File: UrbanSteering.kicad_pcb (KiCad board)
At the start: 2 copper layers, 144 x 78 mm, 30 parts, among them J1 DMS, J2 MAINPLUG, J3 BRAKE+THROTTLE, J4 STM32L432, J5 2.2TFT, U1 MCP2562

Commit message: started pcb layout
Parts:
- removed H7, H8: MountingHole_Pad, MountingHole:MountingHole_3.2mm_M3_Pad
- removed S6: CAN_RESISTOR_SW, dip_swtich_1pos:SW_DS04-254-2-01BK-SMT
- removed TP1: DMS2, TestPoint:TestPoint_THTPad_D4.0mm_Drill2.0mm
- removed TP3: 3V3, TestPoint:TestPoint_THTPad_D4.0mm_Drill2.0mm
- removed TP4: GND, TestPoint:TestPoint_THTPad_D4.0mm_Drill2.0mm
- removed TP5: CAN_H, TestPoint:TestPoint_THTPad_D4.0mm_Drill2.0mm
- removed TP6: CAN_L, TestPoint:TestPoint_THTPad_D4.0mm_Drill2.0mm
- removed TP7: +5V, TestPoint:TestPoint_THTPad_D4.0mm_Drill2.0mm
- added C1: 0.1uF, Capacitor_SMD:C_0805_2012Metric, F.Cu at (396.8, 104.5)
- added C2: 0.1uF, Capacitor_SMD:C_0805_2012Metric, F.Cu at (388.7, 112.5)
- added C3: 0.1uF, Capacitor_SMD:C_0805_2012Metric, F.Cu at (384.2, 112.5)
- added J10: Conn_01x01_Female, Connector_PinHeader_2.54mm:PinHeader_1x01_P2.54mm_Vertical, F.Cu at (400.2, 98.6)
- added J11: Conn_01x01_Female, Connector_PinHeader_2.54mm:PinHeader_1x01_P2.54mm_Vertical, F.Cu at (420.8, 78.5)
- added J12: Conn_01x01_Female, Connector_PinHeader_2.54mm:PinHeader_1x01_P2.54mm_Vertical, F.Cu at (420.8, 73.8)
- added J13: Conn_01x01_Female, Connector_PinHeader_2.54mm:PinHeader_1x01_P2.54mm_Vertical, F.Cu at (425.5, 73.8)
- added J6: Screen_right, Connector_PinHeader_2.54mm:PinHeader_1x04_P2.54mm_Vertical, F.Cu at (128.9, 76.0)
- added J7: Conn_01x02_Female, Connector_PinHeader_2.54mm:PinHeader_1x02_P2.54mm_Vertical, F.Cu at (411.5, 88.6)
- added J8: Conn_01x01_Female, Connector_PinHeader_2.54mm:PinHeader_1x01_P2.54mm_Vertical, F.Cu at (416.2, 86.1)
- added J9: Proximity_sensor, Supermileage_PCB:705510003, F.Cu at (154.8, 126.5)
- added R10: 68, Resistor_SMD:R_0805_2012Metric, F.Cu at (393.1, 111.7)
- added R11: 68, Resistor_SMD:R_0805_2012Metric, F.Cu at (408.2, 95.0)
- added R12: 68, Resistor_SMD:R_0805_2012Metric, F.Cu at (430.0, 73.0)
- added R13: 220, Resistor_SMD:R_0805_2012Metric, F.Cu at (425.4, 80.6)
- added R14: 10k, Resistor_SMD:R_0805_2012Metric, F.Cu at (420.7, 82.3)
- added R15: 10k, Resistor_SMD:R_0805_2012Metric, F.Cu at (401.2, 105.3)
- added R16: 10k, Resistor_SMD:R_0805_2012Metric, F.Cu at (409.2, 97.9)
- added R4: 10k, Resistor_SMD:R_0805_2012Metric, F.Cu at (434.4, 73.0)
- added R5: 10k, Resistor_SMD:R_0805_2012Metric, F.Cu at (425.4, 77.6)
- added R6: 68, Resistor_SMD:R_0805_2012Metric, F.Cu at (412.7, 95.0)
- added R7: 68, Resistor_SMD:R_0805_2012Metric, F.Cu at (396.8, 107.5)
- added R8: 120, Resistor_SMD:R_0805_2012Metric, F.Cu at (404.7, 97.9)
- added R9: 68, Resistor_SMD:R_0805_2012Metric, F.Cu at (401.2, 102.4)
- added U2: 74HC595PW, Package_SO:TSSOP-16-1EP_4.4x5mm_P0.65mm, F.Cu at (437.7, 97.7)
- added U3: 74HC597D, Package_SO:TSSOP-16-1EP_4.4x5mm_P0.65mm, F.Cu at (386.0, 91.7)
- H1, H2, H3, H4, H5, H6: value MountingHole_Pad -> MountingHole; footprint MountingHole:MountingHole_3.2mm_M3_Pad -> MountingHole:MountingHole_3.2mm_M3
- J1: value DMS -> Joystick; footprint 15-91-2035:15912035 -> Connector_PinHeader_2.54mm:PinHeader_1x05_P2.54mm_Vertical; moved to F.Cu
- J2: value MAINPLUG -> Main_conn; footprint eec:Molex-15-91-2045-0-0-0 -> KiCad:705510007; moved to F.Cu
- J3: value BRAKE+THROTTLE -> CAN_term; footprint eec:Molex-15-91-2045-0-0-0 -> Connector_PinHeader_2.54mm:PinHeader_1x02_P2.54mm_Vertical; moved to F.Cu
- J4: moved to F.Cu
- J5: value 2.2TFT -> Screen_left; footprint schematic:2.2TFT -> Connector_PinHeader_2.54mm:PinHeader_1x14_P2.54mm_Vertical
- R1: value 100K -> 10k; footprint Resistor_SMD:R_0603_1608Metric -> Resistor_SMD:R_0805_2012Metric; moved to F.Cu
- R2: value 100 -> 10k; footprint Resistor_SMD:R_0603_1608Metric -> Resistor_SMD:R_0805_2012Metric; moved to F.Cu
- R3: value 120 -> 10k; footprint Resistor_SMD:R_0603_1608Metric -> Resistor_SMD:R_0805_2012Metric; moved to F.Cu
- moved R1 312.0 mm to (430.0, 75.9), turned to 0 degrees
- moved R3 310.5 mm to (416.1, 89.9), turned to 0 degrees
- moved R2 296.3 mm to (420.7, 85.2), turned to 0 degrees
- moved U1 248.9 mm to (367.1, 109.1)
- moved J3 196.2 mm to (383.6, 99.9), turned to 0 degrees
- moved S5 157.2 mm to (243.0, 71.0)
- moved S3 112.5 mm to (101.0, 80.0)
- moved J4 103.3 mm to (230.0, 140.0), turned to -90 degrees
- moved H6 94.9 mm to (103.0, 147.0)
- moved J5 90.6 mm to (213.2, 63.3)
- moved H5 65.8 mm to (103.0, 126.8)
- moved J2 63.0 mm to (182.0, 126.1)
- moved H4 61.5 mm to (145.0, 120.0)
- moved H1 51.9 mm to (199.0, 120.0)
- moved H2 44.6 mm to (222.0, 74.0)
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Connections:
- net LCD_MISO renamed /LCD_MISO
- net LCD_MOSI renamed /LCD_MOSI
- net LCD_SCK renamed /LCD_SCK
- net RXD renamed /RXD
- net TXD renamed /TXD
- J1 pad 2: DMS -> VCC
- J1 pad 3: +3V3 -> /JoystickX
- J2 pad 1: GND -> Net-(J2-Pad1)
- J2 pad 2: CAN_L -> /Throttle
- J2 pad 3: CAN_H -> GND
- J2 pad 4: +12V -> /CANH
- J3 pad 1: GND -> Net-(J3-Pad1)
- J3 pad 2: Net-(J3-Pad2) -> /CANH
- J4 pad 1: Net-(J3-Pad3) -> Net-(J2-Pad1)
- J4 pad 10: Net-(J4-Pad10) -> unconnected-(J4-Pad10)
- J4 pad 11: Net-(J4-Pad11) -> unconnected-(J4-Pad11)
- J4 pad 12: HAZARDS -> /LCD_CS
- J4 pad 17: +3V3 -> VCC
- J4 pad 18: Net-(J4-Pad18) -> unconnected-(J4-Pad18)
- J4 pad 19: LIGHTS -> /SD_CS
- J4 pad 2: LCD_RST -> /LCD_RST
- J4 pad 20: DMS -> /ProximInput
- J4 pad 21: WIPRERS -> /JoystickY
- J4 pad 22: LCD_DC -> /JoystickX
- J4 pad 23: Net-(J4-Pad23) -> /LCD_DC
- J4 pad 24: Net-(J4-Pad24) -> /ProximLED
- J4 pad 25: Net-(J3-Pad2) -> /Throttle
- J4 pad 26: LCD_CS -> unconnected-(J4-Pad26)
- J4 pad 28: Net-(J4-Pad28) -> unconnected-(J4-Pad28)
- J4 pad 3: Net-(J4-Pad3) -> unconnected-(J4-Pad3)
- J4 pad 6: IND_RIGHT -> /SRCLK
- J4 pad 7: IND_LEFT -> /STM-SR1
- J4 pad 8: HORN -> /Latch
- J4 pad 9: IGNITION -> /SR2-STM
- J5 pad 1: +3V3 -> VCC
- J5 pad 3: LCD_CS -> /LCD_CS
- J5 pad 4: LCD_RST -> /LCD_RST
- J5 pad 5: LCD_DC -> /LCD_DC
- J5 pad 8: LCD_LED -> VCC
- R1 pad 1: +3V3 -> GND
- R1 pad 2: LCD_RST -> /BTN_IND_LEFT
- R2 pad 1: +3V3 -> GND
- R2 pad 2: LCD_LED -> /BTN_LIGHTS
- R3 pad 1: CAN_H -> GND
- R3 pad 2: Net-(R3-Pad2) -> /BTN_IND_RIGHT
- S1 pad 1: +3V3 -> VCC
- S1 pad 2: HORN -> /BTN_HORN
- S1 pad L2: Net-(S1-PadL2) -> unconnected-(S1-PadL2)
- S1 pad LC: Net-(S1-PadLC) -> VCC
- S2 pad 2: +3V3 -> VCC
- S2 pad LEFT: IND_LEFT -> /BTN_IND_LEFT
- S2 pad RIGHT: IND_RIGHT -> /BTN_IND_RIGHT
- S3 pad 1: +3V3 -> VCC
- S3 pad 2: IGNITION -> /BTN_IGNITION
- S3 pad LC: Net-(S3-PadLC) -> VCC
- S4 pad 1: +3V3 -> VCC
- S4 pad 2: WIPRERS -> /BTN_WIPERS
- S4 pad L1: Net-(S4-PadL1) -> unconnected-(S4-PadL1)
- S4 pad LC: Net-(S4-PadLC) -> VCC
- S5 pad 1: +3V3 -> VCC
- S5 pad 2: LIGHTS -> /BTN_LIGHTS
- S5 pad L1: Net-(S5-PadL1) -> unconnected-(S5-PadL1)
- S5 pad LC: Net-(S5-PadLC) -> VCC
- TP2 pad 1: +3V3 -> VCC
- TP2 pad 2: HAZARDS -> /BTN_HAZARDS
- TP2 pad L2: Net-(TP2-PadL2) -> unconnected-(TP2-PadL2)
- TP2 pad LC: Net-(TP2-PadLC) -> VCC
- U1 pad 5: +3V3 -> VCC
- U1 pad 6: CAN_L -> /CANL
- U1 pad 7: CAN_H -> /CANH
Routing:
- net +3V3: track 416.9 -> 0.00 mm, vias 4 -> 0
- net IND_LEFT: track 108.4 -> 0.00 mm
- net /LCD_MISO: track 98.9 -> 0.00 mm, vias 1 -> 0
- net /LCD_MOSI: track 94.4 -> 0.00 mm, vias 1 -> 0
- net IND_RIGHT: track 90.6 -> 0.00 mm
- net Net-(J3-Pad2): track 84.4 -> 0.00 mm
- net +5V: track 82.7 -> 0.00 mm, vias 2 -> 0
- net Net-(J3-Pad3): track 73.7 -> 0.00 mm
- net +12V: track 73.4 -> 0.00 mm
- net LIGHTS: track 69.8 -> 0.00 mm
- net /TXD: track 65.4 -> 0.00 mm
- net LCD_RST: track 65.4 -> 0.00 mm, vias 2 -> 0
- net HORN: track 61.2 -> 0.00 mm
- net HAZARDS: track 60.0 -> 0.00 mm
- net CAN_H: track 55.7 -> 0.00 mm, vias 2 -> 0
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- removed copper zone on B.Cu, net GND
- removed copper zone on F.Cu, net GND
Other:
- board size 144 x 78 mm -> 344.7 x 105.6 mm
- net class Default removed

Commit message: PCB version-4 layout 1.0
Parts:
- U1: moved to F.Cu
- moved J8 310.9 mm to (107.0, 52.9)
- moved J11 310.8 mm to (111.1, 52.9)
- moved J7 310.7 mm to (102.7, 54.7), turned to 180 degrees
- moved J13 307.0 mm to (119.2, 52.9)
- moved J12 306.4 mm to (115.2, 52.9)
- moved R1 276.2 mm to (153.9, 70.2)
- moved R3 268.3 mm to (148.5, 70.2)
- moved R11 262.3 mm to (148.5, 58.8)
- moved R6 261.1 mm to (154.1, 58.5)
- moved R8 258.2 mm to (148.7, 64.1)
- moved R4 258.0 mm to (176.5, 68.2)
- moved R16 257.1 mm to (154.3, 64.1)
- moved U2 255.8 mm to (182.0, 89.7)
- moved R14 250.1 mm to (171.4, 62.8)
- moved R5 248.7 mm to (176.7, 73.2)
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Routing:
- net GND: track 0.00 -> 462.8 mm, vias 0 -> 30
- net VCC: track 0.00 -> 452.7 mm, vias 0 -> 19
- net /ProximInput: track 0.00 -> 267.4 mm, vias 0 -> 5
- net /CANH: track 0.00 -> 229.9 mm, vias 0 -> 4
- net /LCD_SCK: track 0.00 -> 214.1 mm, vias 0 -> 2
- net +12V: track 0.00 -> 212.2 mm, vias 0 -> 2
- net +5V: track 0.00 -> 178.0 mm, vias 0 -> 9
- net /CANL: track 0.00 -> 150.1 mm, vias 0 -> 14
- net /LCD_MISO: track 0.00 -> 146.6 mm, vias 0 -> 4
- net /LCD_MOSI: track 0.00 -> 142.3 mm, vias 0 -> 4
- net /BTN_HORN: track 0.00 -> 138.6 mm, vias 0 -> 4
- net /BTN_LIGHTS: track 0.00 -> 121.3 mm, vias 0 -> 9
- net /SD_CS: track 0.00 -> 120.8 mm
- net /BTN_HAZARDS: track 0.00 -> 116.2 mm, vias 0 -> 6
- net Net-(R9-Pad2): track 0.00 -> 113.4 mm, vias 0 -> 2
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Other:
- board size 344.7 x 105.6 mm -> 144 x 100 mm

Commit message: PCB version 4 layout 2.0
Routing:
- net /BTN_IGNITION: track 54.6 -> 146.1 mm, vias 0 -> 6
- net /BTN_HAZARDS: track 116.2 -> 169.3 mm, vias 6 -> 11
- net /BTN_WIPERS: track 109.0 -> 137.7 mm, vias 8 -> 12
- net /SW_JOY: track 85.2 -> 111.3 mm, vias 4 -> 7
- net VCC: track 452.7 -> 476.2 mm, vias 19 -> 26
- net /LED_IGNITION_ON: track 64.4 -> 67.7 mm
- net /LCD_SCK: track 214.1 -> 215.0 mm
- net Net-(J9-Pad1): track 91.9 -> 92.7 mm
- net /LCD_MISO: track 146.6 -> 147.1 mm

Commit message: PCB version 4 layout 3.0
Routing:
- net GND: track 462.8 -> 479.6 mm
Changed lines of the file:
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@@
   (segment (start 153.419979 62.77354) (end 152.955179 62.30874) (width 0.25) (layer "F.Cu") (net 1))
   (segment (start 228.697979 132.38) (end 225.024139 136.05384) (width 0.25) (layer "F.Cu") (net 1))
+  (segment (start 117.225 60.275) (end 118.35 61.4) (width 0.25) (layer "F.Cu") (net 1))
   (segment (start 176.92 125.821519) (end 178.456779 124.28474) (width 0.25) (layer "F.Cu") (net 1))
   (segment (start 147.624979 70.18274) (end 147.624979 71.647847) (width 0.25) (layer "F.Cu") (net 1))
@@
   (segment (start 152.193179 69.41694) (end 152.958979 70.18274) (width 0.25) (layer "F.Cu") (net 1))
   (segment (start 176.92 126.12724) (end 176.92 125.821519) (width 0.25) (layer "F.Cu") (net 1))
+  (segment (start 103.675 60.275) (end 117.225 60.275) (width 0.25) (layer "F.Cu") (net 1))
   (segment (start 179.213979 93.15474) (end 179.213979 91.94324) (width 0.25) (layer "F.Cu") (net 1))
   (segment (start 185.619579 123.97994) (end 184.095579 122.45594) (width 0.25) (layer "F.Cu") (net 1))
@@
   (segment (start 156.517779 122.20194) (end 159.305179 122.20194) (width 0.25) (layer "F.Cu") (net 1))
   (segment (start 153.419979 64.08674) (end 152.142379 65.36434) (width 0.25) (layer "F.Cu") (net 1))
+  (segment (start 102.55 61.4) (end 103.675 60.275) (width 0.25) (layer "F.Cu") (net 1))
   (segment (start 176.932779 124.64034) (end 176.932779 126.114461) (width 0.25) (layer "F.Cu") (net 1))
   (segment (start 120.798779 65.30594) (end 120.092839 64.6) (width 0.25) (layer "F.Cu") (net 1))

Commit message: adjusts position of some footprints, adds most required labels, deletes existing traces, flips LCD orientation, and adjusts netclass sizes
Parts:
- H1, H2, H3, H4, H5, H6: value MountingHole -> M3
- J2: footprint KiCad:705510007 -> Connector_Molex:705510007
- J5: value Screen_left -> Screen_Left
- J6: value Screen_right -> Screen_Right
- J9: footprint Supermileage_PCB:705510003 -> Connector_Molex:705510003
- TP1: renamed from J7; value Conn_01x02_Female -> CAN
- TP2: renamed from J8; value Conn_01x01_Female -> Proxim
- TP3: renamed from J10; value Conn_01x01_Female -> 3v3
- TP4: renamed from J11; value Conn_01x01_Female -> 12v
- TP5: renamed from J12; value Conn_01x01_Female -> 5v
- TP6: renamed from J13; value Conn_01x01_Female -> GND
- moved TP4 102.1 mm to (191.7, 115.7)
- moved TP5 93.4 mm to (184.2, 115.9)
- moved TP3 89.5 mm to (176.8, 115.9)
- moved TP1 86.0 mm to (161.8, 117.1)
- moved J6 85.3 mm to (214.2, 73.7)
- moved J5 83.4 mm to (129.8, 61.0)
- moved R8 81.0 mm to (191.0, 133.2), turned to 180 degrees
- moved TP6 80.8 mm to (169.7, 116.1)
- moved TP2 79.0 mm to (154.1, 116.4)
- moved R13 74.5 mm to (204.7, 138.1), turned to 180 degrees
- moved J3 74.0 mm to (211.0, 123.6)
- moved R6 39.2 mm to (185.9, 81.4), turned to 180 degrees
- moved R5 38.7 mm to (139.9, 85.0)
- moved R11 37.5 mm to (186.0, 61.0), turned to 180 degrees
- moved C1 34.9 mm to (189.3, 94.6), turned to -90 degrees
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- renumbered TP2 to S6
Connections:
- J1 pad 1: GND -> /SW_JOY
- J1 pad 2: VCC -> /JoystickY
- J1 pad 4: /JoystickY -> VCC
- J1 pad 5: /SW_JOY -> GND
- R5 pad 1: /SW_JOY -> VCC
- R5 pad 2: VCC -> /SW_JOY
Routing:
- net GND: track 479.6 -> 0.00 mm, vias 30 -> 0
- net VCC: track 476.2 -> 0.00 mm, vias 26 -> 0
- net /ProximInput: track 267.7 -> 0.00 mm, vias 5 -> 0
- net /CANH: track 229.9 -> 0.00 mm, vias 4 -> 0
- net /LCD_SCK: track 215.0 -> 0.00 mm, vias 2 -> 0
- net +12V: track 212.2 -> 0.00 mm, vias 2 -> 0
- net +5V: track 178.0 -> 0.00 mm, vias 9 -> 0
- net /BTN_HAZARDS: track 169.3 -> 0.00 mm, vias 11 -> 0
- net /CANL: track 150.1 -> 0.00 mm, vias 14 -> 0
- net /LCD_MISO: track 147.1 -> 0.00 mm, vias 4 -> 0
- net /BTN_IGNITION: track 146.1 -> 0.00 mm, vias 6 -> 0
- net /LCD_MOSI: track 142.3 -> 0.00 mm, vias 4 -> 0
- net /BTN_HORN: track 138.6 -> 0.00 mm, vias 4 -> 0
- net /BTN_WIPERS: track 137.7 -> 0.00 mm, vias 12 -> 0
- net /BTN_LIGHTS: track 121.3 -> 0.00 mm, vias 9 -> 0
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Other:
- outline, holes or cut-outs redrawn
- board text added: "3v3"
- board text added: "GND"
- board text added: "LED"
- board text added: "Prox"
- board text removed: "UBCSupermileage_UrbanSteering_V3.0"

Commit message: makes bottom filled zone GND and adds some connections from top SMD component grounds
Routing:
- net GND: track 0.00 -> 33.8 mm, vias 0 -> 1
- added copper zone on B.Cu, net GND
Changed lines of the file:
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@@
     (effects (font (size 1 1) (thickness 0.15)))
   )
+  (segment (start 162.198479 75.57474) (end 165.285979 75.57474) (width 0.5) (layer "F.Cu") (net 1))
+  (segment (start 162.298479 75.47474) (end 162.198479 75.57474) (width 0.5) (layer "F.Cu") (net 1))
+  (segment (start 162.298479 70.37474) (end 162.298479 75.47474) (width 0.5) (layer "F.Cu") (net 1))
+  (segment (start 162.685979 90.46224) (end 162.685979 95.57474) (width 0.5) (layer "F.Cu") (net 1))
+  (segment (start 162.598479 90.37474) (end 162.685979 90.46224) (width 0.5) (layer "F.Cu") (net 1))
+  (segment (start 162.310979 85.28724) (end 162.398479 85.37474) (width 0.5) (layer "F.Cu") (net 1))
+  (segment (start 165.285979 75.57474) (end 165.385979 75.67474) (width 0.5) (layer "F.Cu") (net 1))
+  (segment (start 162.310979 80.57474) (end 162.310979 85.28724) (width 0.5) (layer "F.Cu") (net 1))
+  (segment (start 162.310979 80.57474) (end 162.198479 80.46224) (width 0.5) (layer "F.Cu") (net 1))
+  (segment (start 162.398479 85.37474) (end 162.398479 90.17474) (width 0.5) (layer "F.Cu") (net 1))
+  (segment (start 162.198479 70.27474) (end 162.298479 70.37474) (width 0.5) (layer "F.Cu") (net 1))
+  (segment (start 162.198479 65.27474) (end 162.198479 70.27474) (width 0.5) (layer "F.Cu") (net 1))
+  (segment (start 162.398479 90.17474) (end 162.598479 90.37474) (width 0.5) (layer "F.Cu") (net 1))
+  (segment (start 162.198479 80.46224) (end 162.198479 75.57474) (width 0.5) (layer "F.Cu") (net 1))
+  (via (at 165.385979 75.67474) (size 1) (drill 0.5) (layers "F.Cu" "B.Cu") (net 1))
+  (zone (net 1) (net_name "GND") (layer "B.Cu") (hatch edge 0.508)
+    (connect_pads (clearance 0.000001))
+    (min_thickness 0.254)
+    (fill (thermal_gap 0.508) (thermal_bridge_width 0.508))
+    (polygon
+      (pts
+        (xy 247.885979 151.67474)
+        (xy 97.385979 154.17474)
+        (xy 97.385979 47.67474)
+        (xy 247.885979 47.17474)
+      )
+    )
+  )
 )

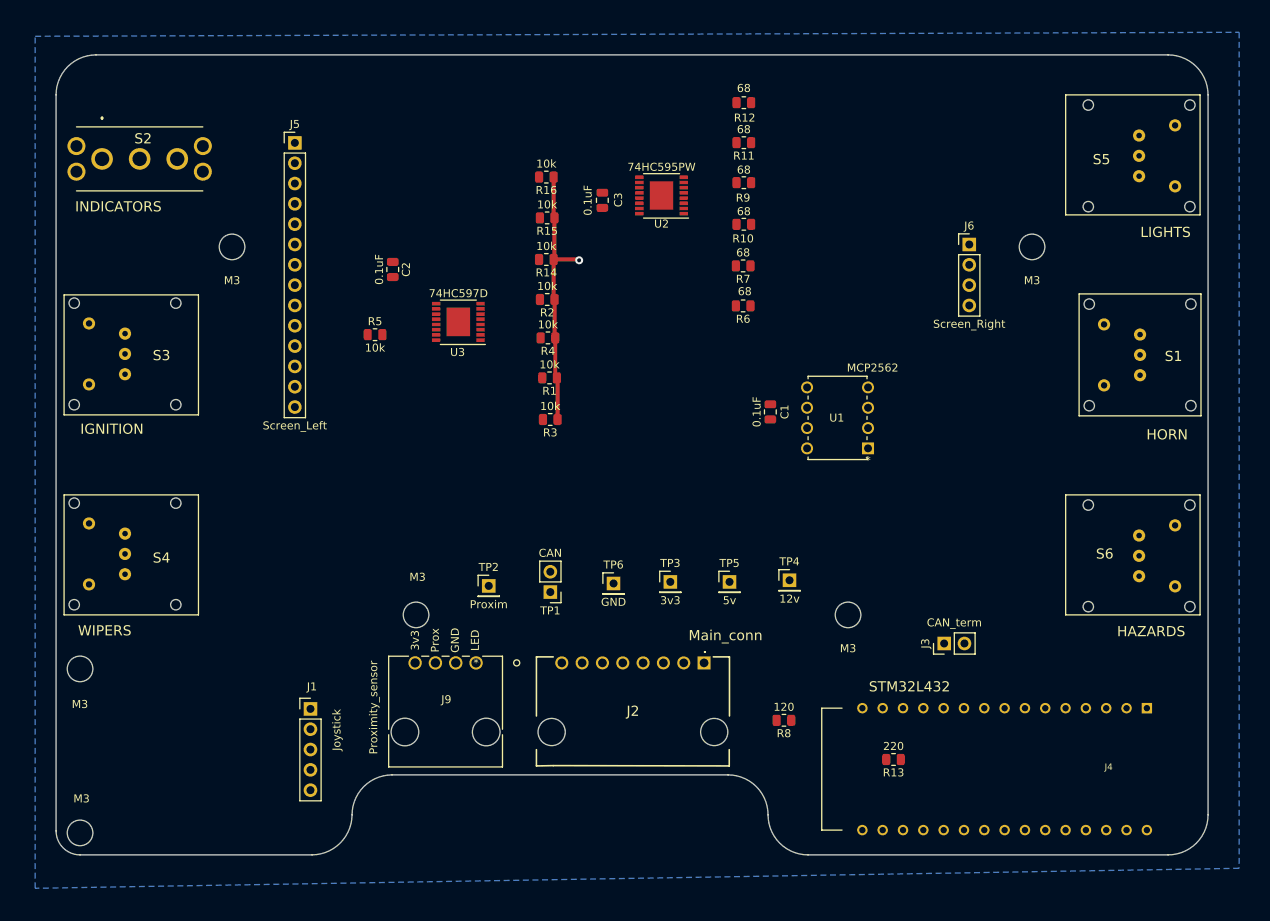
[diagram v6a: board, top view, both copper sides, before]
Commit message: added top filled zone for VCC
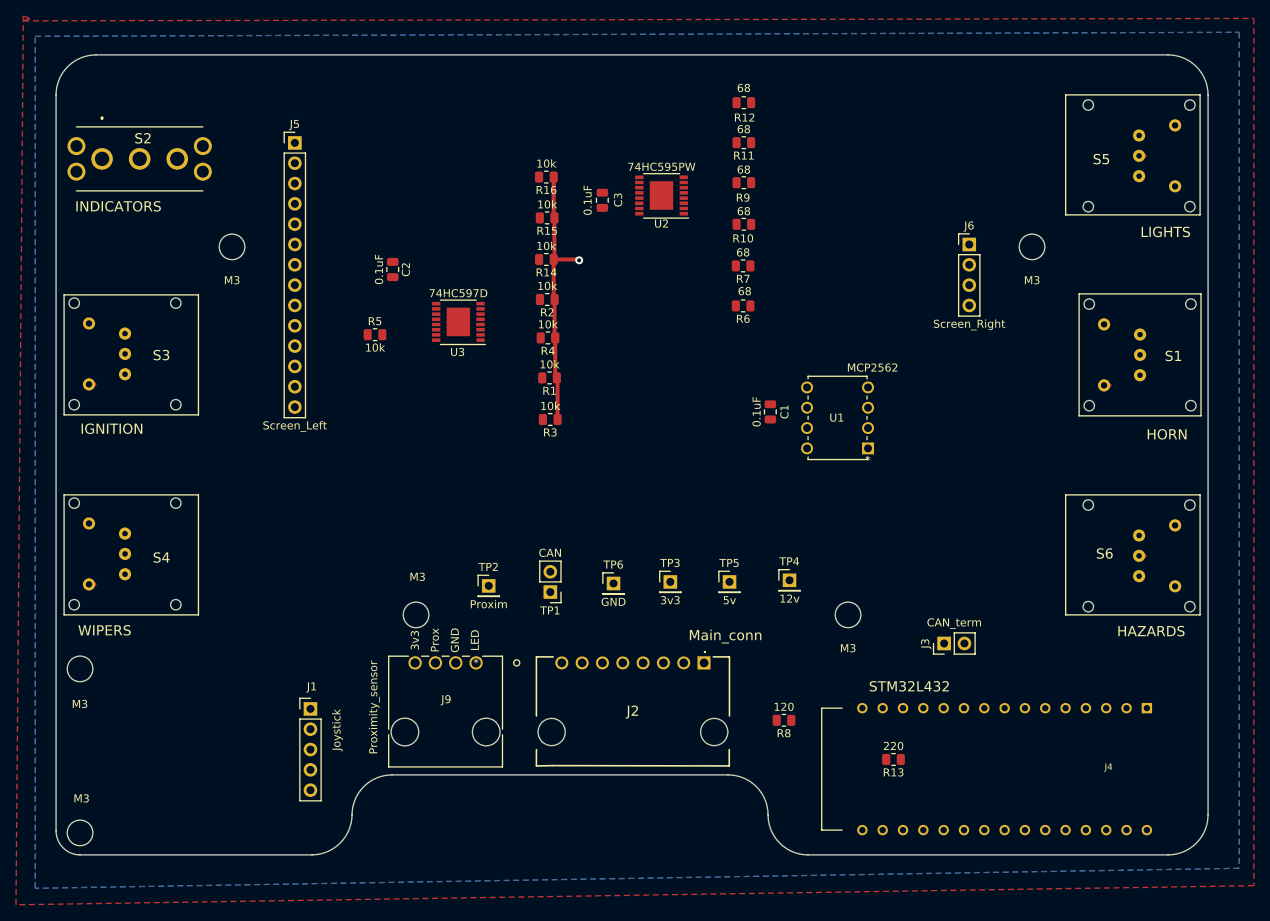
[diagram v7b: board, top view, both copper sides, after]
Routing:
- net VCC: track 0.00 -> 3.45 mm
- added copper zone on F.Cu, net VCC
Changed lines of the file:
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@@
   (segment (start 162.198479 80.46224) (end 162.198479 75.57474) (width 0.5) (layer "F.Cu") (net 1))
   (via (at 165.385979 75.67474) (size 1) (drill 0.5) (layers "F.Cu" "B.Cu") (net 1))
+  (segment (start 236.07 62.62) (end 235.38 62.62) (width 0.5) (layer "F.Cu") (net 3))
+  (segment (start 104.81 116.19) (end 104.12 116.19) (width 0.5) (layer "F.Cu") (net 3))
+  (segment (start 104.81 91.19) (end 104.12 91.19) (width 0.5) (layer "F.Cu") (net 3))
+  (segment (start 236.07 112.62) (end 235.38 112.62) (width 0.5) (layer "F.Cu") (net 3))
+  (segment (start 231.69 91.31) (end 231 91.31) (width 0.5) (layer "F.Cu") (net 3))
+  (zone (net 3) (net_name "VCC") (layer "F.Cu") (hatch edge 0.508)
+    (connect_pads (clearance 0.000001))
+    (min_thickness 0.254) (filled_areas_thickness no)
+    (fill yes (thermal_gap 0.508) (thermal_bridge_width 0.508))
+    (polygon
+      (pts
+        (xy 96.770379 45.44314)
+        (xy 95.906779 45.74794)
+        (xy 249.729179 45.44314)
+        (xy 249.729179 153.85034)
+        (xy 94.992379 156.23794)
+        (xy 95.906779 45.13834)
+      )
+    )
+  )
   (zone (net 1) (net_name "GND") (layer "B.Cu") (hatch edge 0.508)
     (connect_pads (clearance 0.000001))
-    (min_thickness 0.254)
-    (fill (thermal_gap 0.508) (thermal_bridge_width 0.508))
+    (min_thickness 0.254) (filled_areas_thickness no)
+    (fill yes (thermal_gap 0.508) (thermal_bridge_width 0.508))
     (polygon
       (pts

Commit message: added labels and tracing... Some errors on DRC
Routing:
- net /LCD_DC: track 0.00 -> 231.1 mm
- net /LCD_SCK: track 0.00 -> 192.5 mm, vias 0 -> 5
- net /LCD_RST: track 0.00 -> 183.0 mm, vias 0 -> 2
- net /LCD_MISO: track 0.00 -> 180.9 mm, vias 0 -> 9
- net /SRCLK: track 0.00 -> 175.2 mm, vias 0 -> 7
- net +5V: track 0.00 -> 174.1 mm, vias 0 -> 8
- net /BTN_HAZARDS: track 0.00 -> 162.8 mm, vias 0 -> 2
- net /LCD_MOSI: track 0.00 -> 158.6 mm, vias 0 -> 4
- net /Latch: track 0.00 -> 150.6 mm, vias 0 -> 8
- net /LCD_CS: track 0.00 -> 141.7 mm, vias 0 -> 4
- net /SR2-STM: track 0.00 -> 135.8 mm, vias 0 -> 2
- net /BTN_HORN: track 0.00 -> 134.7 mm, vias 0 -> 2
- net /BTN_LIGHTS: track 0.00 -> 125.0 mm
- net Net-(R9-Pad2): track 0.00 -> 116.8 mm, vias 0 -> 4
- net /BTN_IGNITION: track 0.00 -> 109.3 mm, vias 0 -> 8
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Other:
- board text added: "12V"
- board text added: "5V"
- board text added: "Brake"
- board text added: "CANH"
- board text added: "CANL"
- board text added: "JOY_X"
- board text added: "JOY_Y"
- board text added: "Joy_X"
- board text added: "Joy_Y"
- board text added: "LCD_ DC"
- board text added: "LCD_ MOSI"
- board text added: "LCD_ SCK"
- board text added: "LCD_CS"
- board text added: "LCD_DC"
- board text added: "LCD_MISO"
- board text added: "LCD_MOSI"
- board text added: "LCD_RST"
- board text added: "LCD_SCK"
- board text added: "Latch"
- board text added: "Prox Input"
- board text added: "Prox LED"
- board text added: "RXD"
- board text added: "SD_ CS"
- board text added: "SR2_STM"
- board text added: "SRCLK"
- board text added: "STM-SR1"
- board text added: "SW_JOY"
- board text added: "TXD"
- board text added: "Throttle"
- board text added: "VCC"
- board text added: "x"
